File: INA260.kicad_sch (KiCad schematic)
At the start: 2 parts, among them U2 INA260AIPWR

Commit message: Separate PCBs into individual repos to allow for multiple workgroups
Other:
- title: HEDGE2 Avionics -> HEDGE2 OBC
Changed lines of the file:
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@@
 	(paper "USLedger")
 	(title_block
-		(title "HEDGE2 Avionics")
+		(title "HEDGE2 OBC")
 		(date "2025-06-27")
 		(rev "V0.8")
@@
 		)
 		(instances
-			(project "Avionics"
+			(project "HEDGE2-OBC"
 				(path "/ace5002f-3cbc-4a0a-869b-0e31ebd905b7/893aef5a-59ff-410b-9a71-9930aaf04e9f/740c0668-bfac-47e0-b7b8-de442260ca55"
 					(reference "C3")
@@
 		)
 		(instances
-			(project "Avionics"
+			(project "HEDGE2-OBC"
 				(path "/ace5002f-3cbc-4a0a-869b-0e31ebd905b7/893aef5a-59ff-410b-9a71-9930aaf04e9f/740c0668-bfac-47e0-b7b8-de442260ca55"
 					(reference "#PWR066")
@@
 		)
 		(instances
-			(project "Avionics"
+			(project "HEDGE2-OBC"
 				(path "/ace5002f-3cbc-4a0a-869b-0e31ebd905b7/893aef5a-59ff-410b-9a71-9930aaf04e9f/740c0668-bfac-47e0-b7b8-de442260ca55"
 					(reference "U2")
@@
 		)
 		(instances
-			(project "Avionics"
+			(project "HEDGE2-OBC"
 				(path "/ace5002f-3cbc-4a0a-869b-0e31ebd905b7/893aef5a-59ff-410b-9a71-9930aaf04e9f/740c0668-bfac-47e0-b7b8-de442260ca55"
 					(reference "#PWR065")

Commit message: Cleanup after splitting PCBs into separate repos
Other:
- title: HEDGE2 OBC -> HEDGE-2 OBC
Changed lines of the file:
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@@
 	(paper "USLedger")
 	(title_block
-		(title "HEDGE2 OBC")
-		(date "2025-06-27")
-		(rev "V0.8")
+		(title "HEDGE-2 OBC")
+		(date "2025-09-08")
+		(rev "V1.0")
 		(company "University of Virginia")
 		(comment 1 "Department of Mechanical and Aerospace Engineering")
@@
 		(instances
 			(project "HEDGE2-OBC"
-				(path "/ace5002f-3cbc-4a0a-869b-0e31ebd905b7/893aef5a-59ff-410b-9a71-9930aaf04e9f/740c0668-bfac-47e0-b7b8-de442260ca55"
+				(path "/a13a6ce3-91ba-42e3-9b40-443fe6a0f2d9/740c0668-bfac-47e0-b7b8-de442260ca55"
+					(reference "C4")
+					(unit 1)
+				)
+				(path "/a13a6ce3-91ba-42e3-9b40-443fe6a0f2d9/9fa6cc5e-a76a-4d58-8af7-47af14171882"
 					(reference "C3")
-					(unit 1)
-				)
-				(path "/ace5002f-3cbc-4a0a-869b-0e31ebd905b7/893aef5a-59ff-410b-9a71-9930aaf04e9f/9fa6cc5e-a76a-4d58-8af7-47af14171882"
-					(reference "C8")
 					(unit 1)
 				)
@@
 		(dnp no)
 		(fields_autoplaced yes)
-		(property "Reference" "#PWR066"
+		(property "Reference" "#PWR047"
 			(at 231.14 152.4 0)
 			(effects
@@
 		(instances
 			(project "HEDGE2-OBC"
-				(path "/ace5002f-3cbc-4a0a-869b-0e31ebd905b7/893aef5a-59ff-410b-9a71-9930aaf04e9f/740c0668-bfac-47e0-b7b8-de442260ca55"
-					(reference "#PWR066")
+				(path "/a13a6ce3-91ba-42e3-9b40-443fe6a0f2d9/740c0668-bfac-47e0-b7b8-de442260ca55"
+					(reference "#PWR049")
 					(unit 1)
 				)
-				(path "/ace5002f-3cbc-4a0a-869b-0e31ebd905b7/893aef5a-59ff-410b-9a71-9930aaf04e9f/9fa6cc5e-a76a-4d58-8af7-47af14171882"
-					(reference "#PWR072")
+				(path "/a13a6ce3-91ba-42e3-9b40-443fe6a0f2d9/9fa6cc5e-a76a-4d58-8af7-47af14171882"
+					(reference "#PWR047")
 					(unit 1)
 				)
@@
 		(instances
 			(project "HEDGE2-OBC"
-				(path "/ace5002f-3cbc-4a0a-869b-0e31ebd905b7/893aef5a-59ff-410b-9a71-9930aaf04e9f/740c0668-bfac-47e0-b7b8-de442260ca55"
+				(path "/a13a6ce3-91ba-42e3-9b40-443fe6a0f2d9/740c0668-bfac-47e0-b7b8-de442260ca55"
+					(reference "U3")
+					(unit 1)
+				)
+				(path "/a13a6ce3-91ba-42e3-9b40-443fe6a0f2d9/9fa6cc5e-a76a-4d58-8af7-47af14171882"
 					(reference "U2")
-					(unit 1)
-				)
-				(path "/ace5002f-3cbc-4a0a-869b-0e31ebd905b7/893aef5a-59ff-410b-9a71-9930aaf04e9f/9fa6cc5e-a76a-4d58-8af7-47af14171882"
-					(reference "U4")
 					(unit 1)
 				)
@@
 		(dnp no)
 		(fields_autoplaced yes)
-		(property "Reference" "#PWR065"
+		(property "Reference" "#PWR046"
 			(at 182.88 93.98 0)
 			(effects
@@
 		(instances
 			(project "HEDGE2-OBC"
-				(path "/ace5002f-3cbc-4a0a-869b-0e31ebd905b7/893aef5a-59ff-410b-9a71-9930aaf04e9f/740c0668-bfac-47e0-b7b8-de442260ca55"
-					(reference "#PWR065")
+				(path "/a13a6ce3-91ba-42e3-9b40-443fe6a0f2d9/740c0668-bfac-47e0-b7b8-de442260ca55"
+					(reference "#PWR048")
 					(unit 1)
 				)
-				(path "/ace5002f-3cbc-4a0a-869b-0e31ebd905b7/893aef5a-59ff-410b-9a71-9930aaf04e9f/9fa6cc5e-a76a-4d58-8af7-47af14171882"
-					(reference "#PWR071")
+				(path "/a13a6ce3-91ba-42e3-9b40-443fe6a0f2d9/9fa6cc5e-a76a-4d58-8af7-47af14171882"
+					(reference "#PWR046")
 					(unit 1)
 				)

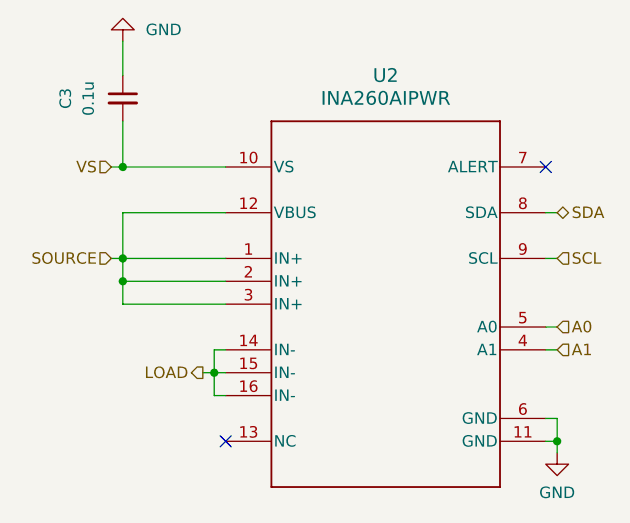
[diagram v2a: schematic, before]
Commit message: Add RS-485 interfaces; modify for 5V power input
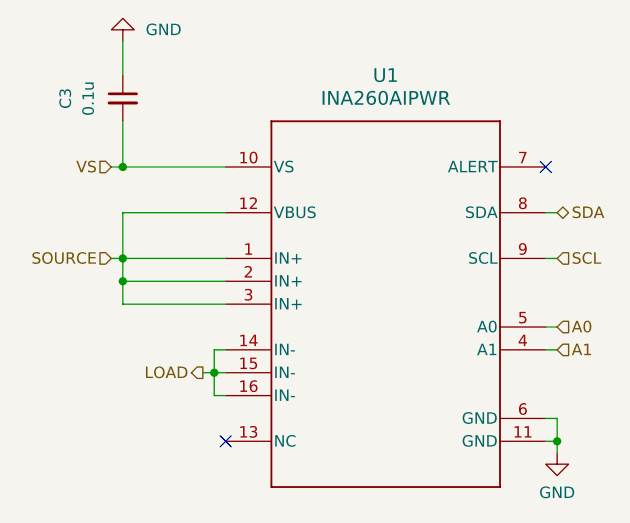
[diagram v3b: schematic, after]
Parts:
- renumbered U2 to U1
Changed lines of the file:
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@@
 		(dnp no)
 		(fields_autoplaced yes)
-		(property "Reference" "#PWR047"
+		(property "Reference" "#PWR041"
 			(at 231.14 152.4 0)
 			(effects
@@
 			(project "HEDGE2-OBC"
 				(path "/a13a6ce3-91ba-42e3-9b40-443fe6a0f2d9/740c0668-bfac-47e0-b7b8-de442260ca55"
-					(reference "#PWR049")
+					(reference "#PWR043")
 					(unit 1)
 				)
 				(path "/a13a6ce3-91ba-42e3-9b40-443fe6a0f2d9/9fa6cc5e-a76a-4d58-8af7-47af14171882"
-					(reference "#PWR047")
+					(reference "#PWR041")
 					(unit 1)
 				)
@@
 		(dnp no)
 		(fields_autoplaced yes)
-		(property "Reference" "U2"
+		(property "Reference" "U1"
 			(at 212.09 104.14 0)
 			(effects
@@
 			(project "HEDGE2-OBC"
 				(path "/a13a6ce3-91ba-42e3-9b40-443fe6a0f2d9/740c0668-bfac-47e0-b7b8-de442260ca55"
-					(reference "U3")
+					(reference "U2")
 					(unit 1)
 				)
 				(path "/a13a6ce3-91ba-42e3-9b40-443fe6a0f2d9/9fa6cc5e-a76a-4d58-8af7-47af14171882"
-					(reference "U2")
+					(reference "U1")
 					(unit 1)
 				)
@@
 		(dnp no)
 		(fields_autoplaced yes)
-		(property "Reference" "#PWR046"
+		(property "Reference" "#PWR040"
 			(at 182.88 93.98 0)
 			(effects
@@
 			(project "HEDGE2-OBC"
 				(path "/a13a6ce3-91ba-42e3-9b40-443fe6a0f2d9/740c0668-bfac-47e0-b7b8-de442260ca55"
-					(reference "#PWR048")
+					(reference "#PWR042")
 					(unit 1)
 				)
 				(path "/a13a6ce3-91ba-42e3-9b40-443fe6a0f2d9/9fa6cc5e-a76a-4d58-8af7-47af14171882"
-					(reference "#PWR046")
-					(unit 1)
-				)
+					(reference "#PWR040")
+					(unit 1)
+				)
